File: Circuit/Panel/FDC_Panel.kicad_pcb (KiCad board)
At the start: 2 copper layers, 38 x 58 mm, 11 parts, among them J1 Interconnect, J2 Screen, SW1 Push

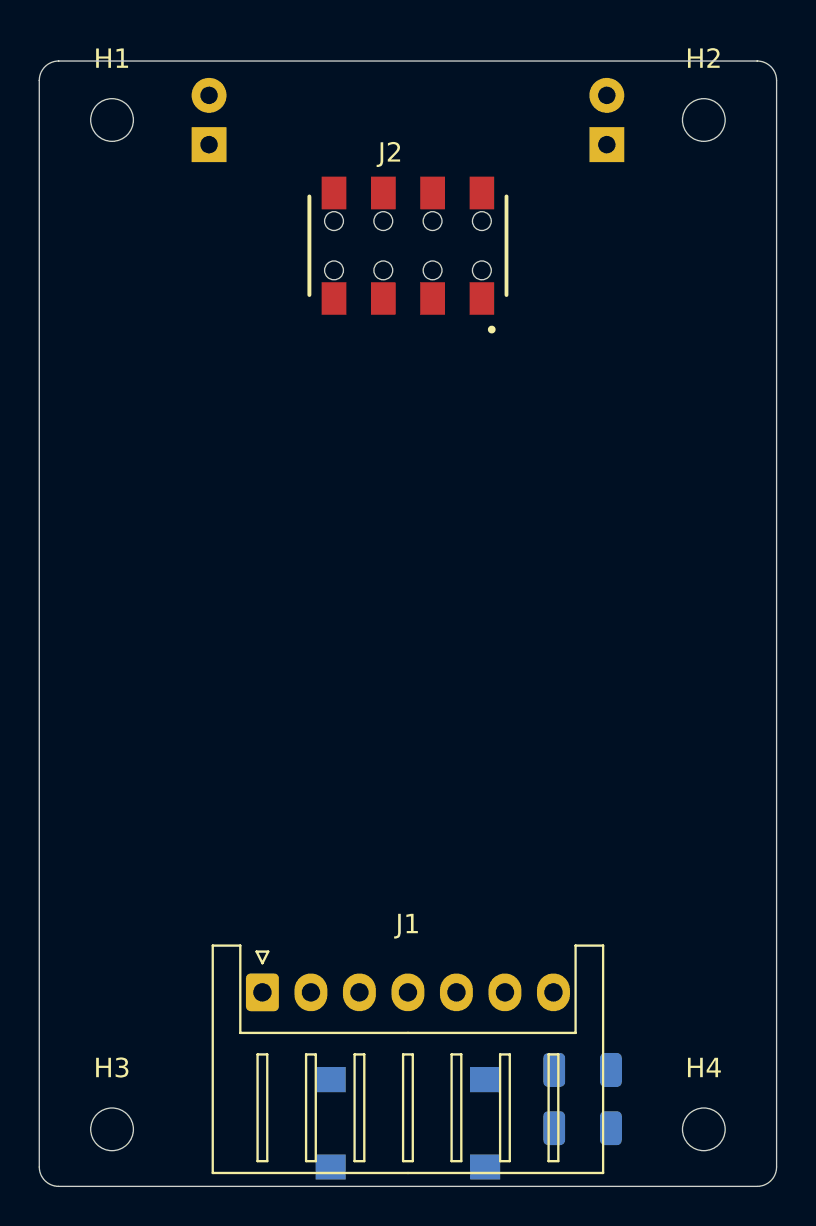
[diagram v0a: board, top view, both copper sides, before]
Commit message: Panel PCB almost done.
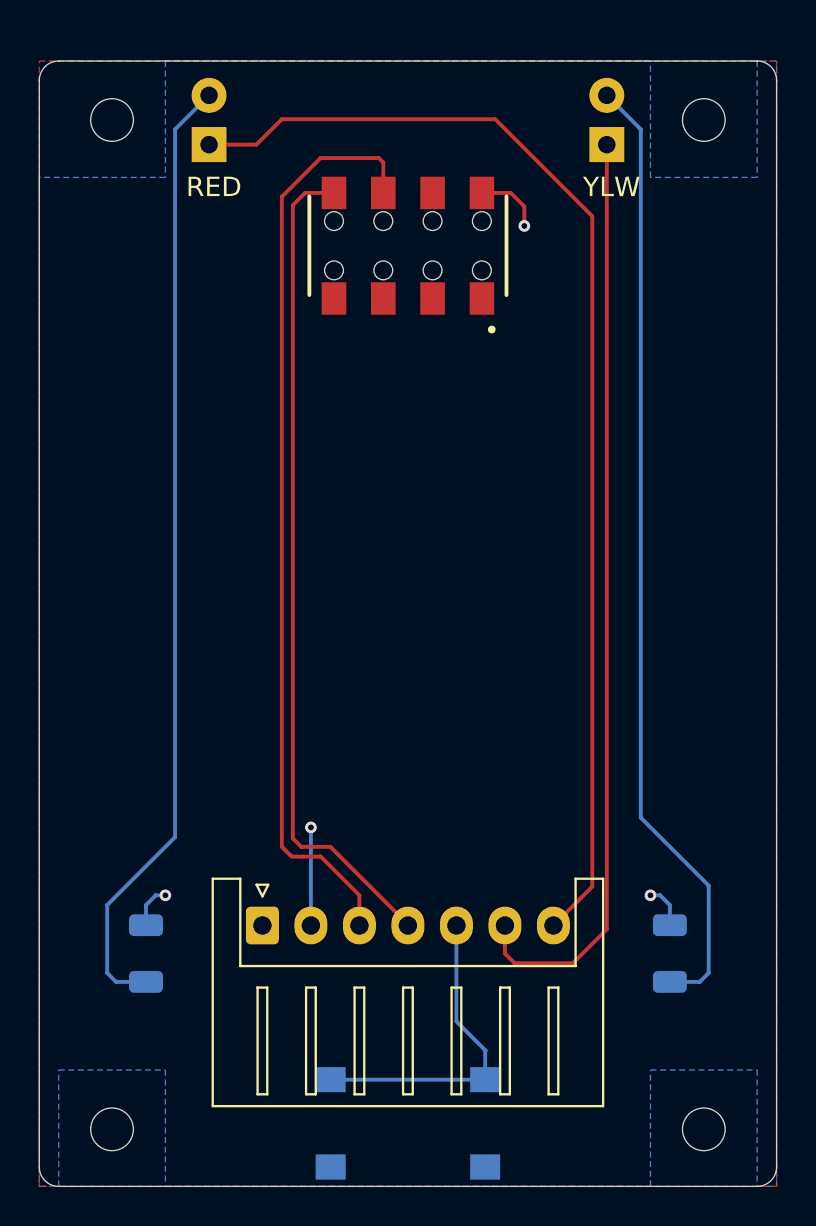
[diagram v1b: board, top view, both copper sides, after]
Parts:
- moved R1 24.2 mm to (30.9, 71.4), turned to -90 degrees
- moved R2 7.50 mm to (57.9, 71.4), turned to -90 degrees
- moved J1 3.45 mm to (36.9, 70.0)
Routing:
- net /Red: track 0.00 -> 59.7 mm
- net Net-(D2-A): track 0.00 -> 49.6 mm
- net Net-(D1-A): track 0.00 -> 49.6 mm
- net /Ylw: track 0.00 -> 47.9 mm
- net /pSDA: track 0.00 -> 47.8 mm
- net /pSCL: track 0.00 -> 42.8 mm
- net /pButt: track 0.00 -> 16.5 mm
- net +5V: track 0.00 -> 9.54 mm, vias 0 -> 3
- net GND: track 0.00 -> 3.48 mm, vias 0 -> 1
- added copper zone on F.Cu, net +5V
- added copper zone on B.Cu, net GND
